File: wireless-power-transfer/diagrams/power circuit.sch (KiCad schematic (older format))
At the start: 15 parts, among them Q1 IRFP260N, Q2 IRFP260N, Q3 IRFP260N, Q4 IRFP260N, T1 CoupledInductor

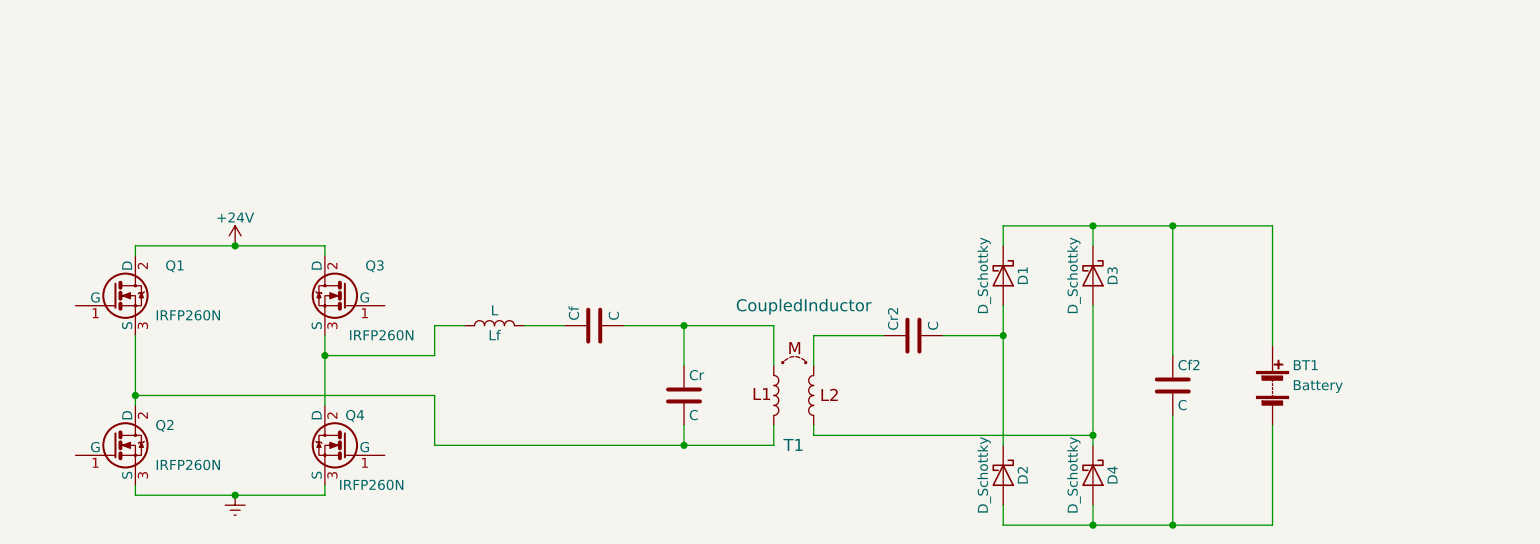
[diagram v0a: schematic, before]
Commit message: Added pdf sheets and modified layout according with the school standard for TFGs.
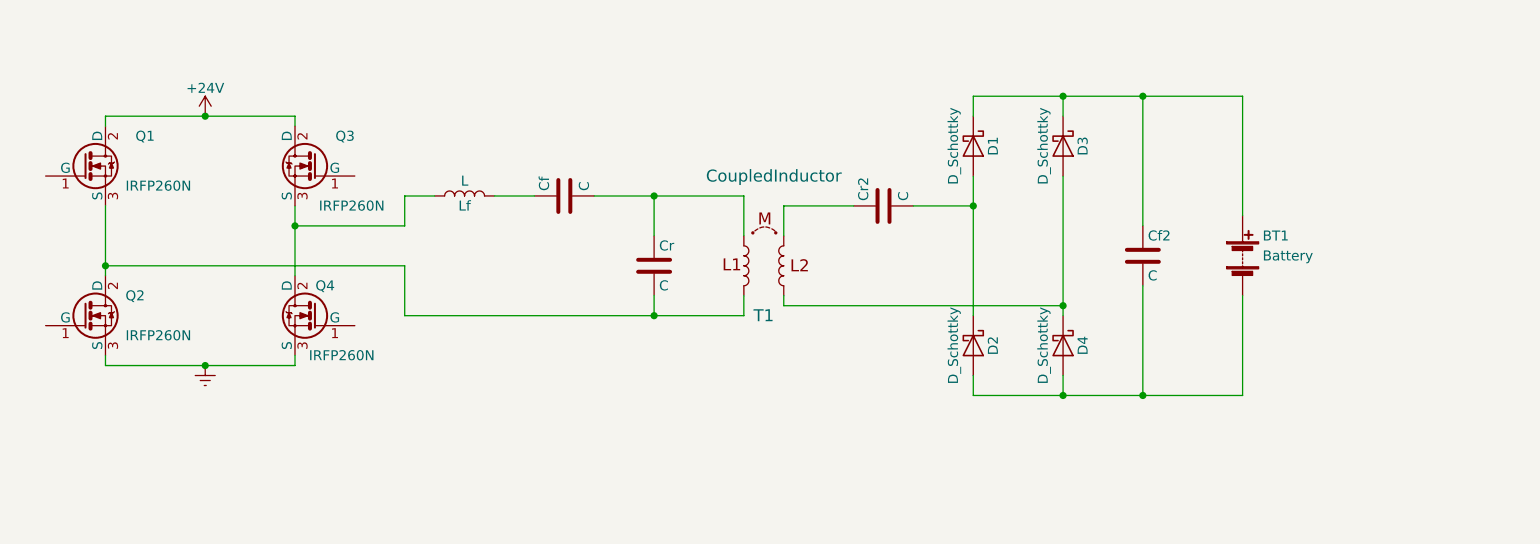
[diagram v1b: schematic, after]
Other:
- moved on the sheet: BT1, Cf, Cf2, Cr, Cr2, D1, D2, D3, D4, Lf, Q1, Q2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

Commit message: Power circuit diagram modified with some text-based explanations.
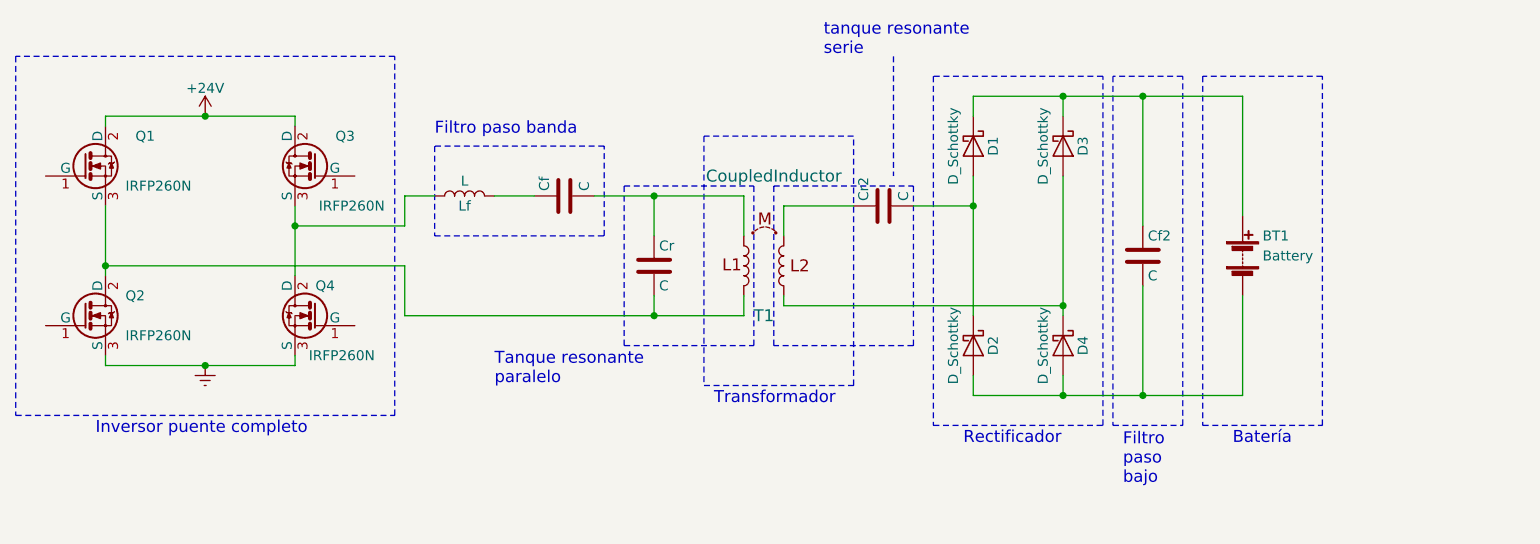
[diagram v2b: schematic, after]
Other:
- note added: "Batería"
- note added: "Filtro paso banda"
- note added: "Filtro\npaso\nbajo"
- note added: "Inversor puente completo"
- note added: "Rectificador"
- note added: "Tanque resonante\nparalelo"
- note added: "Transformador"
- note added: "tanque resonante\nserie"
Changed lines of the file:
@@
 	2750 3800 3700 3800
 Connection ~ 3250 3800
+Wire Notes Line
+	2300 2250 2300 4050
+Wire Notes Line
+	2300 4050 4200 4050
+Wire Notes Line
+	4200 4050 4200 2250
+Wire Notes Line
+	4200 2250 2300 2250
+Wire Notes Line
+	4400 2700 4400 3150
+Wire Notes Line
+	4400 3150 5250 3150
+Wire Notes Line
+	5250 3150 5250 2700
+Wire Notes Line
+	5250 2700 4400 2700
+Wire Notes Line
+	5350 3700 6000 3700
+Wire Notes Line
+	5350 3700 5350 2900
+Wire Notes Line
+	5350 2900 6000 2900
+Wire Notes Line
+	6000 2900 6000 3700
+Wire Notes Line
+	6100 2900 6800 2900
+Wire Notes Line
+	6800 2900 6800 3700
+Wire Notes Line
+	6800 3700 6100 3700
+Wire Notes Line
+	6100 3700 6100 2900
+Wire Notes Line
+	5750 2650 5750 3900
+Wire Notes Line
+	5750 3900 6500 3900
+Wire Notes Line
+	6500 3900 6500 2650
+Wire Notes Line
+	6500 2650 5750 2650
+Wire Notes Line
+	6900 2350 6900 4100
+Wire Notes Line
+	6900 4100 7750 4100
+Wire Notes Line
+	7750 4100 7750 2350
+Wire Notes Line
+	7750 2350 6900 2350
+Wire Notes Line
+	7800 2350 7800 4100
+Wire Notes Line
+	7800 4100 8150 4100
+Wire Notes Line
+	8150 4100 8150 2350
+Wire Notes Line
+	8150 2350 7800 2350
+Wire Notes Line
+	8250 2350 8250 4100
+Wire Notes Line
+	8250 4100 8850 4100
+Wire Notes Line
+	8850 4100 8850 2350
+Wire Notes Line
+	8850 2350 8250 2350
+Text Notes 2700 4150 0    60   ~ 0
+Inversor puente completo
+Text Notes 4400 2650 0    60   ~ 0
+Filtro paso banda
+Text Notes 4700 3900 0    60   ~ 0
+Tanque resonante\nparalelo
+Text Notes 5800 4000 0    60   ~ 0
+Transformador
+Text Notes 6350 2250 0    60   ~ 0
+tanque resonante\nserie
+Wire Notes Line
+	6700 2250 6700 2850
+Text Notes 7050 4200 0    60   ~ 0
+Rectificador
+Text Notes 7850 4400 0    60   ~ 0
+Filtro\npaso\nbajo
+Text Notes 8400 4200 0    60   ~ 0
+Batería
 $EndSCHEMATC

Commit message: Adding some drawings.
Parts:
- added U1: LM7812, symbol LM7812
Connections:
- net at Cf2.1, D1.1 (K), D3.1 (K): now also U1.VI; no longer BT1.1 (+)
- net at BT1.2 (-), Cf2.2, D2.2 (A)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: now also U1.GND
- new net: BT1.1 (+), U1.VO
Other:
- note added: "Cargador de baterías\n"
- note added: "Regulador"
- note removed: "Batería"
- moved on the sheet: BT1
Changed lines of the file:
@@
 	7100 2550 7100 2450
-Wire Wire Line
-	7100 2450 8450 2450
 Wire Wire Line
 	7550 2450 7550 2550
@@
 	7100 3850 7100 3950
 Wire Wire Line
-	7100 3950 8450 3950
+	7100 3950 9000 3950
 Wire Wire Line
 	7550 3950 7550 3850
@@
 L Battery BT1
 U 1 1 59E9CF4F
-P 8450 3250
-F 0 "BT1" H 8550 3350 50  0000 L CNN
-F 1 "Battery" H 8550 3250 50  0000 L CNN
-F 2 "" V 8450 3310 50  0001 C CNN
-F 3 "" V 8450 3310 50  0001 C CNN
-	1    8450 3250
+P 9000 3250
+F 0 "BT1" H 9100 3350 50  0000 L CNN
+F 1 "Battery" H 9100 3250 50  0000 L CNN
+F 2 "" V 9000 3310 50  0001 C CNN
+F 3 "" V 9000 3310 50  0001 C CNN
+	1    9000 3250
 	1    0    0    -1
 $EndComp
 Wire Wire Line
-	8450 2450 8450 3050
+	9000 2450 9000 3050
 Connection ~ 7950 2450
 Wire Wire Line
-	8450 3950 8450 3450
+	9000 3950 9000 3450
 Connection ~ 7950 3950
 Wire Wire Line
@@
 Connection ~ 3250 3800
 Wire Notes Line
-	2300 2250 2300 4050
-Wire Notes Line
-	2300 4050 4200 4050
-Wire Notes Line
 	4200 4050 4200 2250
-Wire Notes Line
-	4200 2250 2300 2250
 Wire Notes Line
 	4400 2700 4400 3150
@@
 	8150 2350 7800 2350
 Wire Notes Line
-	8250 2350 8250 4100
+	8800 2350 8800 4100
 Wire Notes Line
-	8250 4100 8850 4100
+	8800 4100 9400 4100
 Wire Notes Line
-	8850 4100 8850 2350
+	9400 4100 9400 2350
 Wire Notes Line
-	8850 2350 8250 2350
+	9400 2350 8800 2350
 Text Notes 2700 4150 0    60   ~ 0
 Inversor puente completo
@@
 Text Notes 7850 4400 0    60   ~ 0
 Filtro\npaso\nbajo
-Text Notes 8400 4200 0    60   ~ 0
-Batería
+Text Notes 8650 4200 0    60   ~ 0
+Cargador de baterías\n
+Wire Wire Line
+	8850 2450 9000 2450
+Wire Wire Line
+	7100 2450 8050 2450
+Wire Notes Line
+	8200 2250 8200 2800
+Wire Notes Line
+	8200 2800 8750 2800
+Wire Notes Line
+	8750 2800 8750 2250
+Wire Notes Line
+	8750 2250 8200 2250
+Wire Wire Line
+	8450 2750 8450 3950
+Connection ~ 8450 3950
+$Comp
+L LM7812 U1
+U 1 1 5A744BE2
+P 8450 2500
+F 0 "U1" H 8575 2300 50  0000 C CNN
+F 1 "LM7812" H 8450 2700 50  0000 C CNN
+F 2 "" H 8450 2500 50  0001 C CNN
+F 3 "" H 8450 2500 50  0001 C CNN
+	1    8450 2500
+	1    0    0    -1
+$EndComp
+Text Notes 8250 2900 0    60   ~ 0
+Regulador
+Wire Notes Line
+	4200 2250 2400 2250
+Wire Notes Line
+	2400 2250 2400 4050
+Wire Notes Line
+	2400 4050 4200 4050
 $EndSCHEMATC
